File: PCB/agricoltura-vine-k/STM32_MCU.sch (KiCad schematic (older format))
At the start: 33 parts, among them SW1 TL3301NF260QG, T1 BU2032SM-JJ-GTR, T2 20021121-00010C4LF, T3 0675031020, U1 STM32F446RET6, X1 ABM3B-8.000MHZ-B2-T, X2 ABS07-32.768KHZ-9-T

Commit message: PCB Routing PRogress
5th relay added to schematic, PCB section with Relays routed, still need to connecto IO expander channels.
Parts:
- removed R2, R4: RC0402FR-074K7L, AVR-KiCAD-Lib-Resistors:R0402, symbol AVR-KiCAD-Lib-Resistors:RC0402FR-074K7L
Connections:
- wire segments 130 -> 125
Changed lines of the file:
@@
 Text HLabel 1200 1850 0    50   Input ~ 0
 RS485_UART_RX2
-Wire Wire Line
-	6650 2150 8550 2150
-$Comp
-L AVR-KiCAD-Lib-Resistors:RC0402FR-074K7L R2
-U 1 1 5EFBBB92
-P 8550 1550
-F 0 "R2" V 8504 1638 50  0000 L CNN
-F 1 "RC0402FR-074K7L" V 8550 1637 50  0001 L CNN
-F 2 "AVR-KiCAD-Lib-Resistors:R0402" H 8550 1550 50  0001 C CNN
-F 3 "https://www.yageo.com/upload/media/product/productsearch/datasheet/rchip/PYu-RC_Group_51_RoHS_L_10.pdf" H 8550 1550 50  0001 C CNN
-F 4 "0.10000" H 8650 1800 50  0001 C CNN "Cost QTY: 1"
-F 5 "0.00289" H 8750 1900 50  0001 C CNN "Cost QTY: 1000"
-F 6 "0.00251" H 8850 2000 50  0001 C CNN "Cost QTY: 2500"
-F 7 "0.00207" H 8950 2100 50  0001 C CNN "Cost QTY: 5000"
-F 8 "0.00163" H 9050 2200 50  0001 C CNN "Cost QTY: 10000"
-F 9 "Yageo" H 9150 2300 50  0001 C CNN "MFR"
-F 10 "RC0402FR-074K7L" H 9250 2400 50  0001 C CNN "MFR#"
-F 11 "Digikey" H 9350 2500 50  0001 C CNN "Vendor"
-F 12 "311-4.7KLRCT-ND" H 9450 2600 50  0001 C CNN "Vendor #"
-F 13 "AVR" H 9550 2700 50  0001 C CNN "Designer"
-F 14 "0.4mm" H 9650 2800 50  0001 C CNN "Height"
-F 15 "12/11/2019" H 10750 3900 50  0001 C CNN "Date Created"
-F 16 "12/11/2019" H 9750 2900 50  0001 C CNN "Date Modified"
-F 17 "Yes" H 9850 3000 50  0001 C CNN "Lead-Free ?"
-F 18 "1" H 9950 3100 50  0001 C CNN "RoHS Levels"
-F 19 "SMT" H 10050 3200 50  0001 C CNN "Mounting"
-F 20 "2" H 10150 3300 50  0001 C CNN "Pin Count #"
-F 21 "Active" H 10250 3400 50  0001 C CNN "Status"
-F 22 "1%" H 10350 3500 50  0001 C CNN "Tolerance"
-F 23 "Thick Film Resistor" H 10450 3600 50  0001 C CNN "Type"
-F 24 "*" H 10550 3700 50  0001 C CNN "Voltage"
-F 25 "0402" H 10650 3850 50  0001 C CNN "Package"
-F 26 "4.7K" V 8595 1638 50  0000 L CNN "_Value_"
-F 27 "*" H 10950 4150 50  0001 C CNN "Management_ID"
-F 28 "4.7 kOhms ±1% 0.063W, 1/16W Chip Resistor 0402 (1005 Metric) Moisture Resistant Thick Film" H 10950 4150 50  0001 C CNN "Description"
-	1    8550 1550
-	0    1    1    0
-$EndComp
-$Comp
-L AVR-KiCAD-Lib-Resistors:RC0402FR-074K7L R4
-U 1 1 5EFBE139
-P 8900 1550
-F 0 "R4" V 8854 1638 50  0000 L CNN
-F 1 "RC0402FR-074K7L" V 8900 1637 50  0001 L CNN
-F 2 "AVR-KiCAD-Lib-Resistors:R0402" H 8900 1550 50  0001 C CNN
-F 3 "https://www.yageo.com/upload/media/product/productsearch/datasheet/rchip/PYu-RC_Group_51_RoHS_L_10.pdf" H 8900 1550 50  0001 C CNN
-F 4 "0.10000" H 9000 1800 50  0001 C CNN "Cost QTY: 1"
-F 5 "0.00289" H 9100 1900 50  0001 C CNN "Cost QTY: 1000"
-F 6 "0.00251" H 9200 2000 50  0001 C CNN "Cost QTY: 2500"
-F 7 "0.00207" H 9300 2100 50  0001 C CNN "Cost QTY: 5000"
-F 8 "0.00163" H 9400 2200 50  0001 C CNN "Cost QTY: 10000"
-F 9 "Yageo" H 9500 2300 50  0001 C CNN "MFR"
-F 10 "RC0402FR-074K7L" H 9600 2400 50  0001 C CNN "MFR#"
-F 11 "Digikey" H 9700 2500 50  0001 C CNN "Vendor"
-F 12 "311-4.7KLRCT-ND" H 9800 2600 50  0001 C CNN "Vendor #"
-F 13 "AVR" H 9900 2700 50  0001 C CNN "Designer"
-F 14 "0.4mm" H 10000 2800 50  0001 C CNN "Height"
-F 15 "12/11/2019" H 11100 3900 50  0001 C CNN "Date Created"
-F 16 "12/11/2019" H 10100 2900 50  0001 C CNN "Date Modified"
-F 17 "Yes" H 10200 3000 50  0001 C CNN "Lead-Free ?"
-F 18 "1" H 10300 3100 50  0001 C CNN "RoHS Levels"
-F 19 "SMT" H 10400 3200 50  0001 C CNN "Mounting"
-F 20 "2" H 10500 3300 50  0001 C CNN "Pin Count #"
-F 21 "Active" H 10600 3400 50  0001 C CNN "Status"
-F 22 "1%" H 10700 3500 50  0001 C CNN "Tolerance"
-F 23 "Thick Film Resistor" H 10800 3600 50  0001 C CNN "Type"
-F 24 "*" H 10900 3700 50  0001 C CNN "Voltage"
-F 25 "0402" H 11000 3850 50  0001 C CNN "Package"
-F 26 "4.7K" V 8945 1638 50  0000 L CNN "_Value_"
-F 27 "*" H 11300 4150 50  0001 C CNN "Management_ID"
-F 28 "4.7 kOhms ±1% 0.063W, 1/16W Chip Resistor 0402 (1005 Metric) Moisture Resistant Thick Film" H 11300 4150 50  0001 C CNN "Description"
-	1    8900 1550
-	0    1    1    0
-$EndComp
-Wire Wire Line
-	8550 1750 8550 2150
-Wire Wire Line
-	8900 1750 8900 2250
-Wire Wire Line
-	8900 2250 6650 2250
-Wire Wire Line
-	8550 1350 8900 1350
 $Comp
 L power:+3V3 #PWR09
@@
 	1    0    0    -1
 $EndComp
-$Comp
-L power:+3V3 #PWR015
-U 1 1 5EFCA33E
-P 8550 1350
-F 0 "#PWR015" H 8550 1200 50  0001 C CNN
-F 1 "+3V3" H 8565 1523 50  0000 C CNN
-F 2 "" H 8550 1350 50  0001 C CNN
-F 3 "" H 8550 1350 50  0001 C CNN
-	1    8550 1350
-	1    0    0    -1
-$EndComp
-Connection ~ 8550 1350
 Wire Wire Line
 	4800 1550 1200 1550

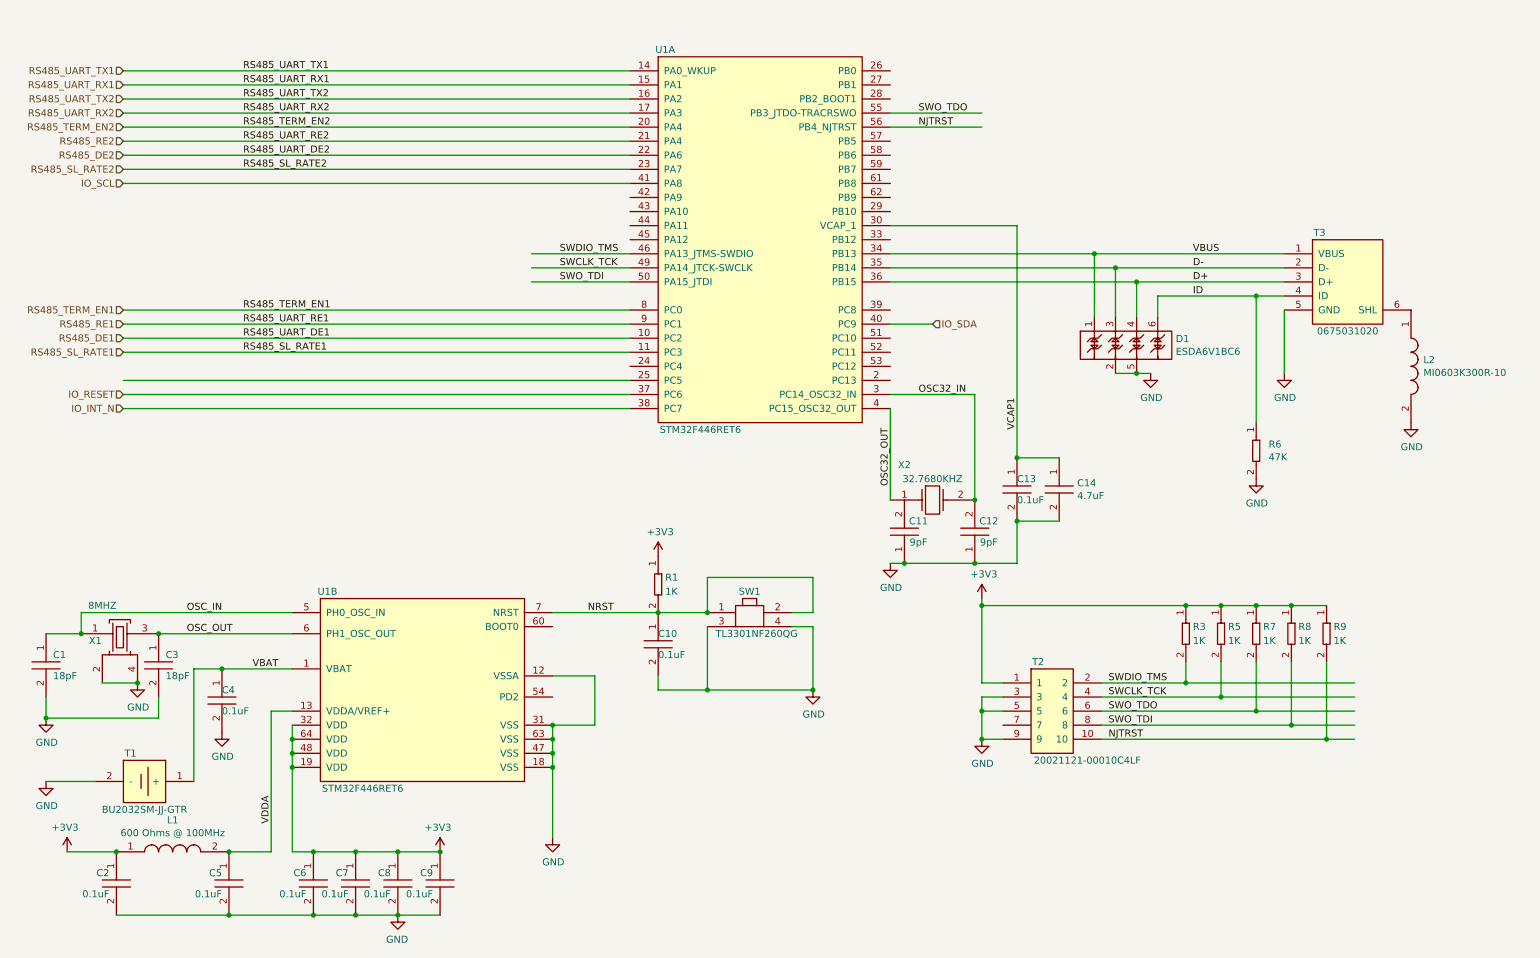
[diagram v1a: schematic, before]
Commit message: EEPROM
added EEPROM to IO expander serial port. Broke out remaining IO expander pins to header. Adjusted silkscreen labeling and reset button position to match the other Vine.
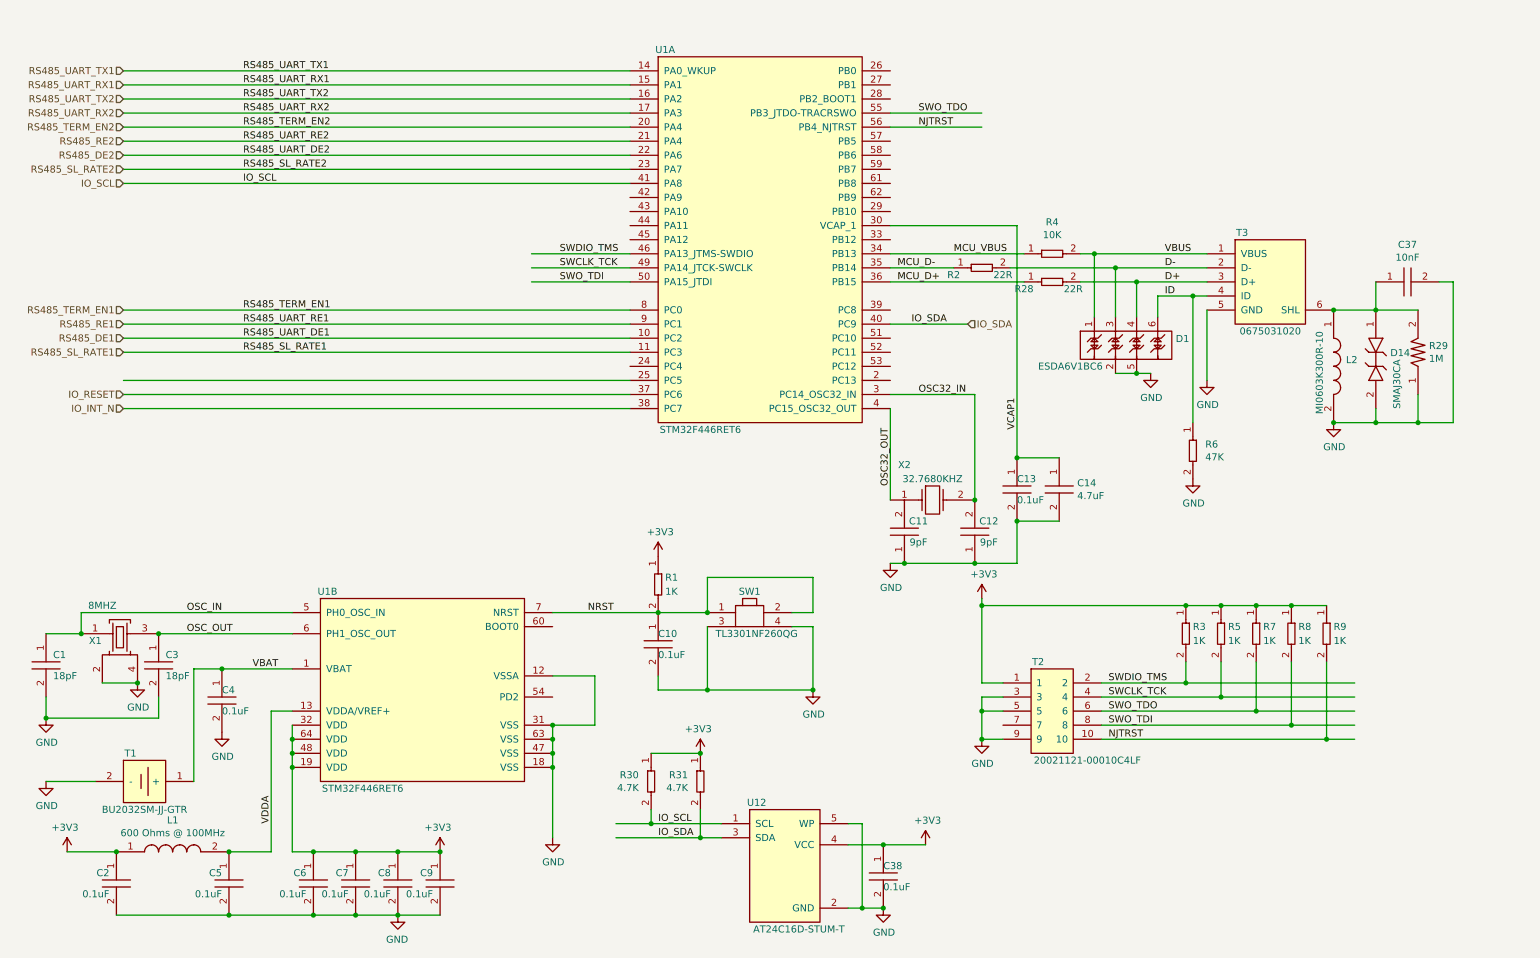
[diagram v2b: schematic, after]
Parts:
- added C37: C0805C103KCRACAUTO, AVR-KiCAD-Lib-Capacitors:C0805, symbol AVR-KiCAD-Lib-Capacitors:C0805C103KCRACAUTO
- added C38: C0402C104K9PACTU, AVR-KiCAD-Lib-Resistors:R0402, symbol AVR-KiCAD-Lib-Capacitors:C0402C104K9PACTU
- added D14: SMAJ30CA, AVR-KiCAD-Lib-Diodes:SMAJ30CA, symbol AVR-KiCAD-Lib-Diodes:SMAJ30CA
- added R2, R28: RC0402FR-0722RL, AVR-KiCAD-Lib-Resistors:R0402, symbol AVR-KiCAD-Lib-Resistors:RC0402FR-0722RL
- added R29: RC1206FR-071ML, AVR-KiCAD-Lib-Resistors:R1206, symbol AVR-KiCAD-Lib-Resistors:RC1206FR-071ML
- added R30, R31: RC0402FR-074K7L, AVR-KiCAD-Lib-Resistors:R0402, symbol AVR-KiCAD-Lib-Resistors:RC0402FR-074K7L
- added R4: RC0402FR-0710KL, AVR-KiCAD-Lib-Resistors:R0402, symbol AVR-KiCAD-Lib-Resistors:RC0402FR-0710KL
- added U12: AT24C16D-STUM-T, AVR-KiCAD-Lib-ICs:SOT-23-5, symbol AVR-KiCAD-Lib-ICs:AT24C16D-STUM-T
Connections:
- net labels added: MCU_D+, MCU_D-, MCU_VBUS
- wire segments 125 -> 151
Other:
- moved on the sheet: L2, R6, T3
